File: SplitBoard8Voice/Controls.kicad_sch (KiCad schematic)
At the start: 106 parts, among them SW601 ENV1_B, SW602 ENV2_B, SW603 HP_B, SW604 LFO1_B, SW605 LFO2_B, SW606 HP_B, SW607 LFO3_B, SW608 FF_B, SW609 MIX1_B, SW610 MIX2_B, SW611 ENC_MENU, SW612 ALT_B, U601 MCP23S17_SS, U602 MCP23S17_SS, U603 ILI9341

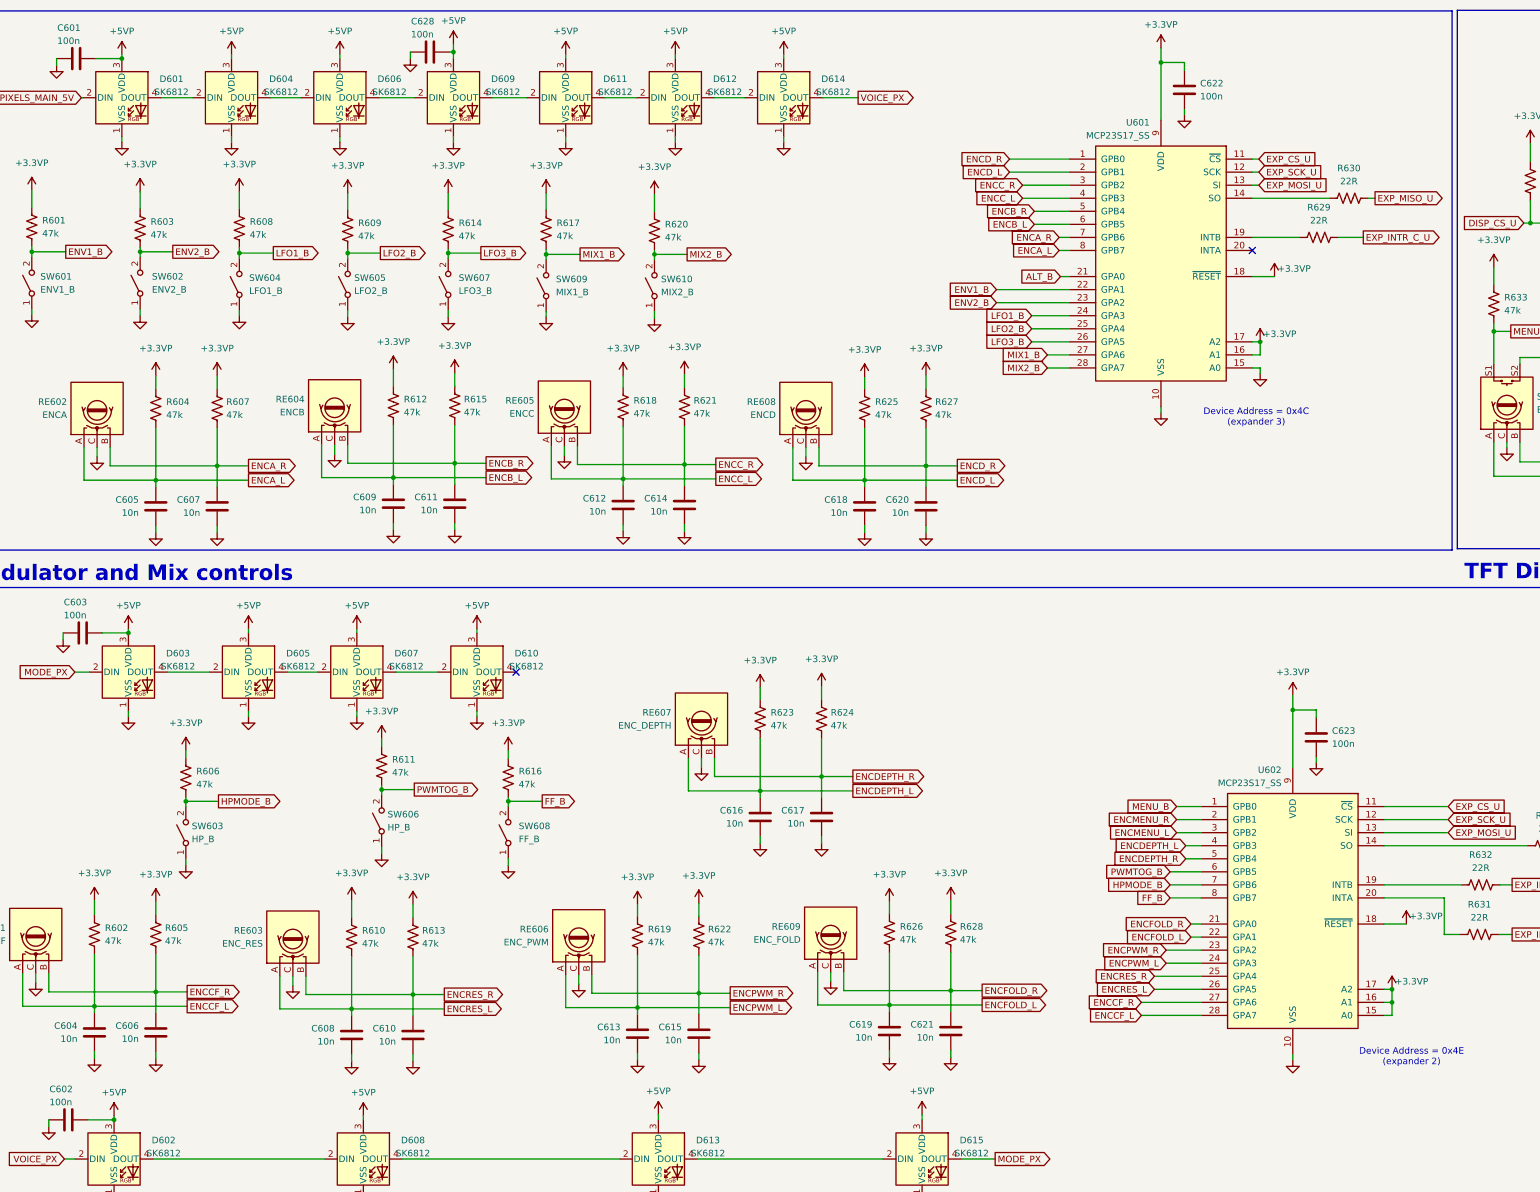
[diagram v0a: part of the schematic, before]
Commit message: back to 3.3v LEDs
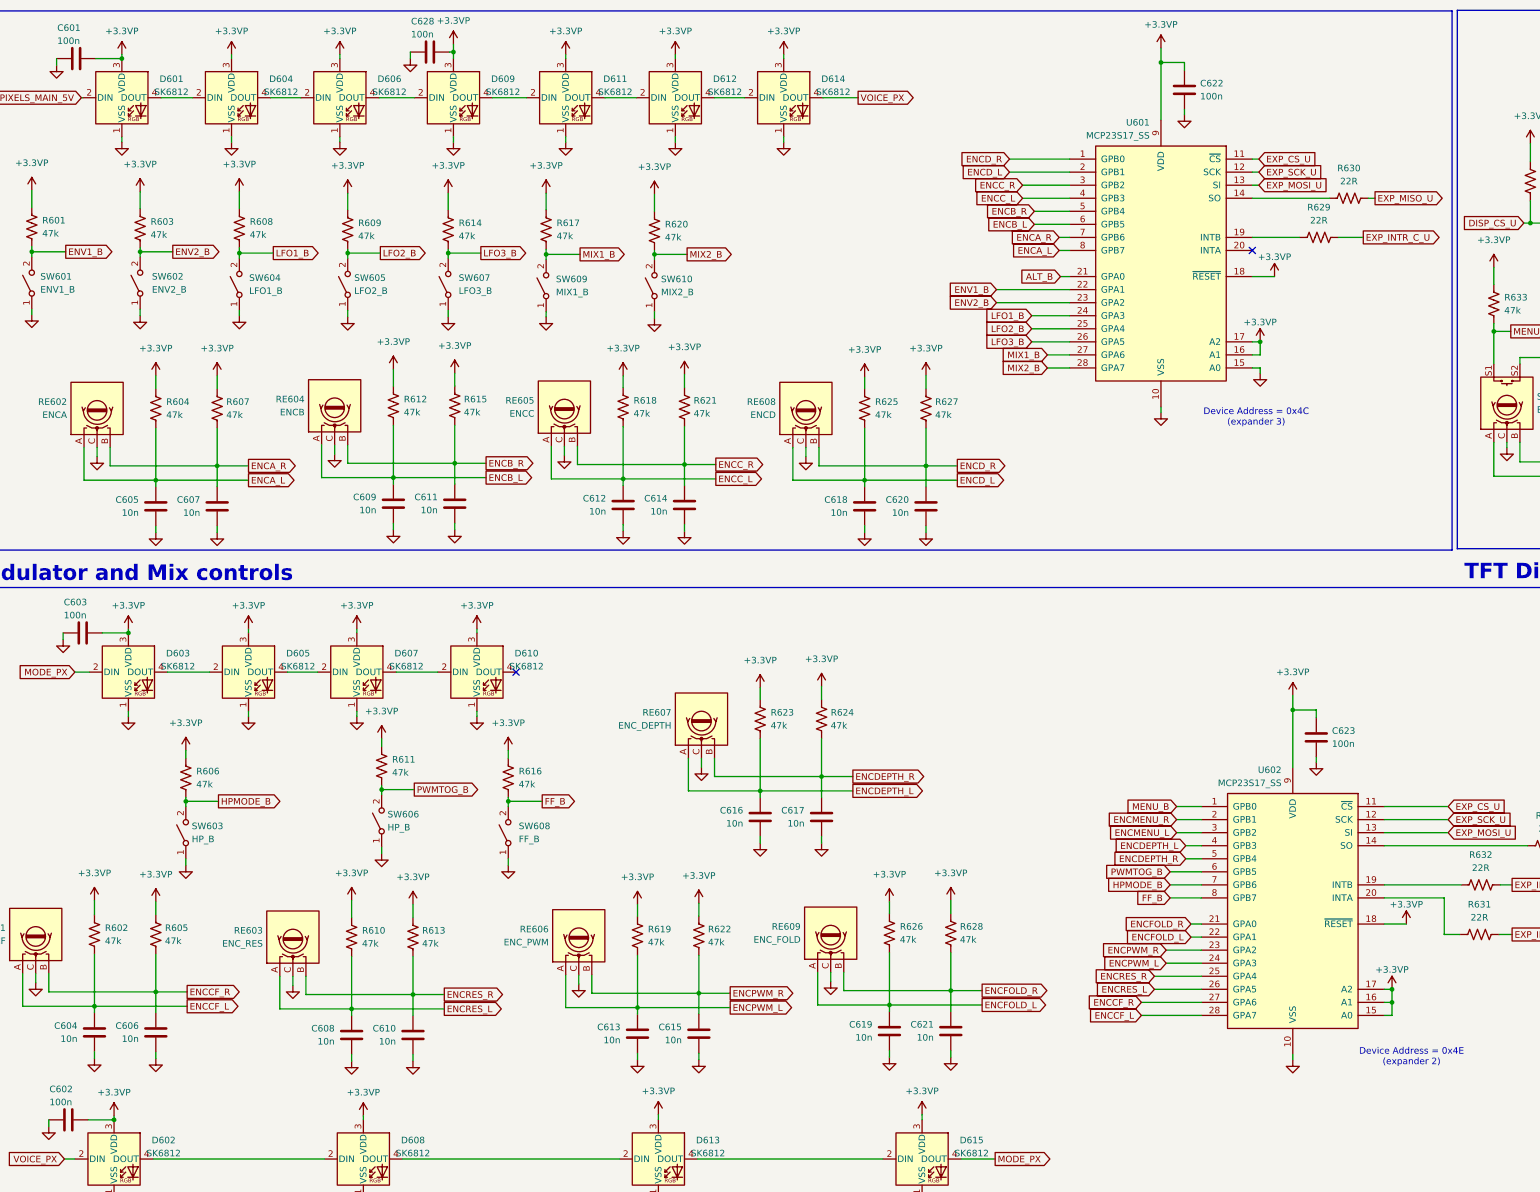
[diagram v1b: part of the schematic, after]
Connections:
- net +5VP is gone; now on net +3.3VP: C601.2, C602.2, C603.2, C628.2, D601.3 (VDD), D602.3 (VDD), D603.3 (VDD), D604.3 (VDD), D605.3 (VDD), D606.3 (VDD), D607.3 (VDD), D608.3 (VDD), D609.3 (VDD), D610.3 (VDD), D611.3 (VDD), D612.3 (VDD), D613.3 (VDD), D614.3 (VDD), D615.3 (VDD)
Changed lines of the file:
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@@
 			)
 		)
-		(property "Value" "+5VP"
+		(property "Value" "+3.3VP"
 			(at 131.064 20.32 0)
 			(effects
@@
 			)
 		)
-		(property "Description" "Power symbol creates a global label with name \"+5VP\""
+		(property "Description" "Power symbol creates a global label with name \"+3.3VP\""
 			(at 131.064 24.892 0)
 			(effects
@@
 			)
 		)
-		(property "Value" "+5VP"
+		(property "Value" "+3.3VP"
 			(at 173.482 20.32 0)
 			(effects
@@
 			)
 		)
-		(property "Description" "Power symbol creates a global label with name \"+5VP\""
+		(property "Description" "Power symbol creates a global label with name \"+3.3VP\""
 			(at 173.482 24.892 0)
 			(effects
@@
 			)
 		)
-		(property "Value" "+5VP"
+		(property "Value" "+3.3VP"
 			(at 91.694 226.822 0)
 			(effects
@@
 			)
 		)
-		(property "Description" "Power symbol creates a global label with name \"+5VP\""
+		(property "Description" "Power symbol creates a global label with name \"+3.3VP\""
 			(at 91.694 231.394 0)
 			(effects
@@
 			)
 		)
-		(property "Value" "+5VP"
+		(property "Value" "+3.3VP"
 			(at 90.424 132.08 0)
 			(effects
@@
 			)
 		)
-		(property "Description" "Power symbol creates a global label with name \"+5VP\""
+		(property "Description" "Power symbol creates a global label with name \"+3.3VP\""
 			(at 90.424 136.652 0)
 			(effects
@@
 			)
 		)
-		(property "Value" "+5VP"
+		(property "Value" "+3.3VP"
 			(at 152.4 20.32 0)
 			(effects
@@
 			)
 		)
-		(property "Description" "Power symbol creates a global label with name \"+5VP\""
+		(property "Description" "Power symbol creates a global label with name \"+3.3VP\""
 			(at 152.4 24.892 0)
 			(effects
@@
 			)
 		)
-		(property "Value" "+5VP"
+		(property "Value" "+3.3VP"
 			(at 43.18 226.822 0)
 			(effects
@@
 			)
 		)
-		(property "Description" "Power symbol creates a global label with name \"+5VP\""
+		(property "Description" "Power symbol creates a global label with name \"+3.3VP\""
 			(at 43.18 231.394 0)
 			(effects
@@
 			)
 		)
-		(property "Value" "+5VP"
+		(property "Value" "+3.3VP"
 			(at 149.098 226.568 0)
 			(effects
@@
 			)
 		)
-		(property "Description" "Power symbol creates a global label with name \"+5VP\""
+		(property "Description" "Power symbol creates a global label with name \"+3.3VP\""
 			(at 149.098 231.14 0)
 			(effects
@@
 			)
 		)
-		(property "Value" "+5VP"
+		(property "Value" "+3.3VP"
 			(at 45.974 132.08 0)
 			(effects
@@
 			)
 		)
-		(property "Description" "Power symbol creates a global label with name \"+5VP\""
+		(property "Description" "Power symbol creates a global label with name \"+3.3VP\""
 			(at 45.974 136.652 0)
 			(effects
@@
 		)
 		(property "Value" "+3.3VP"
-			(at 298.45 192.532 0)
+			(at 294.64 190.246 0)
 			(effects
 				(font
@@
 		)
 		(property "Value" "+3.3VP"
-			(at 295.656 205.232 0)
+			(at 291.846 202.946 0)
 			(effects
 				(font
@@
 		)
 		(property "Value" "+3.3VP"
-			(at 272.796 66.548 0)
+			(at 268.986 64.262 0)
 			(effects
 				(font
@@
 			)
 		)
-		(property "Value" "+5VP"
+		(property "Value" "+3.3VP"
 			(at 69.342 132.08 0)
 			(effects
@@
 			)
 		)
-		(property "Description" "Power symbol creates a global label with name \"+5VP\""
+		(property "Description" "Power symbol creates a global label with name \"+3.3VP\""
 			(at 69.342 136.652 0)
 			(effects
@@
 			)
 		)
-		(property "Value" "+5VP"
+		(property "Value" "+3.3VP"
 			(at 109.22 18.288 0)
 			(effects
@@
 			)
 		)
-		(property "Description" "Power symbol creates a global label with name \"+5VP\""
+		(property "Description" "Power symbol creates a global label with name \"+3.3VP\""
 			(at 109.22 22.86 0)
 			(effects
@@
 			)
 		)
-		(property "Value" "+5VP"
+		(property "Value" "+3.3VP"
 			(at 44.704 20.32 0)
 			(effects
@@
 			)
 		)
-		(property "Description" "Power symbol creates a global label with name \"+5VP\""
+		(property "Description" "Power symbol creates a global label with name \"+3.3VP\""
 			(at 44.704 24.892 0)
 			(effects
@@
 		)
 		(property "Value" "+3.3VP"
-			(at 270.002 79.248 0)
+			(at 266.192 76.962 0)
 			(effects
 				(font
@@
 			)
 		)
-		(property "Value" "+5VP"
+		(property "Value" "+3.3VP"
 			(at 113.792 132.08 0)
 			(effects
@@
 			)
 		)
-		(property "Description" "Power symbol creates a global label with name \"+5VP\""
+		(property "Description" "Power symbol creates a global label with name \"+3.3VP\""
 			(at 113.792 136.652 0)
 			(effects
@@
 			)
 		)
-		(property "Value" "+5VP"
+		(property "Value" "+3.3VP"
 			(at 66.04 20.32 0)
 			(effects
@@
 			)
 		)
-		(property "Description" "Power symbol creates a global label with name \"+5VP\""
+		(property "Description" "Power symbol creates a global label with name \"+3.3VP\""
 			(at 66.04 24.892 0)
 			(effects
@@
 			)
 		)
-		(property "Value" "+5VP"
+		(property "Value" "+3.3VP"
 			(at 200.406 226.568 0)
 			(effects
@@
 			)
 		)
-		(property "Description" "Power symbol creates a global label with name \"+5VP\""
+		(property "Description" "Power symbol creates a global label with name \"+3.3VP\""
 			(at 200.406 231.14 0)
 			(effects
@@
 			)
 		)
-		(property "Value" "+5VP"
+		(property "Value" "+3.3VP"
 			(at 87.122 20.32 0)
 			(effects
@@
 			)
 		)
-		(property "Description" "Power symbol creates a global label with name \"+5VP\""
+		(property "Description" "Power symbol creates a global label with name \"+3.3VP\""
 			(at 87.122 24.892 0)
 			(effects

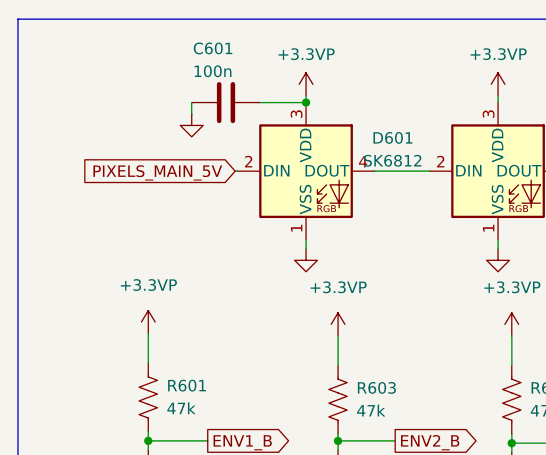
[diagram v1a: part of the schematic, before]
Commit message: upper board routing roughed in
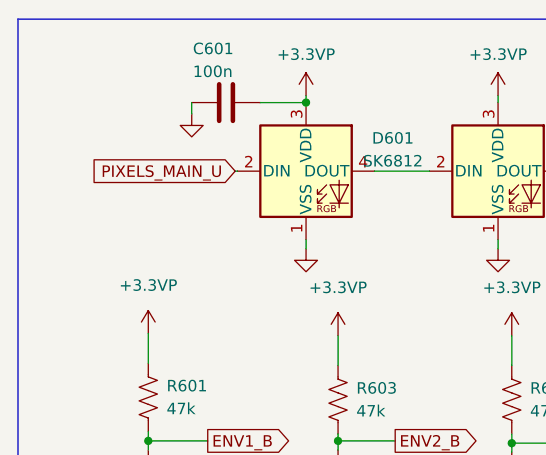
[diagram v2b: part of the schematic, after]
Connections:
- net PIXELS_MAIN_5V renamed PIXELS_MAIN_U
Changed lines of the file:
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@@
 		)
 	)
-	(global_label "PIXELS_MAIN_5V"
+	(global_label "PIXELS_MAIN_U"
 		(shape input)
 		(at 36.83 33.274 180)
@@
 		)
 		(property "Intersheetrefs" "${INTERSHEET_REFS}"
-			(at 18.6653 33.274 0)
+			(at 19.6329 33.274 0)
 			(effects
 				(font

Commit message: larger display footprint
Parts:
- removed U603: ILI9341, Display:TFTBreakout_ILI9341_340x320, symbol Display_Graphic:ILI9314_breakout_9pin
- added U603: ILI9341, Display:TFTBreakout_ILI9341_340x320_86x50mm, symbol Display_Graphic:ILI9314_breakout_14pin
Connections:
- net +3.3VP: now also U603.1 (VCC), U603.8 (LED)
- net DISP_CS_U: now also U603.3 (CS)
- net DISP_DC_U: now also U603.5 (DC/RC)
- net DISP_MOSI_U: now also U603.6 (MOSI)
- net DISP_RST_U: now also U603.4 (RESET)
- net DISP_SCK_U: now also U603.7 (CLK)
- net GNDA: now also U603.2 (GND)
- net at R637.2: now also U603.9 (MISO)
- no-connect marks 2 -> 7
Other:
- moved on the sheet: C623, R631, R632, R635, R639, SW612, U602
